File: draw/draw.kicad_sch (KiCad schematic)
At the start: 7 parts, among them J1 Screw_Terminal_01x03, U1 INA260

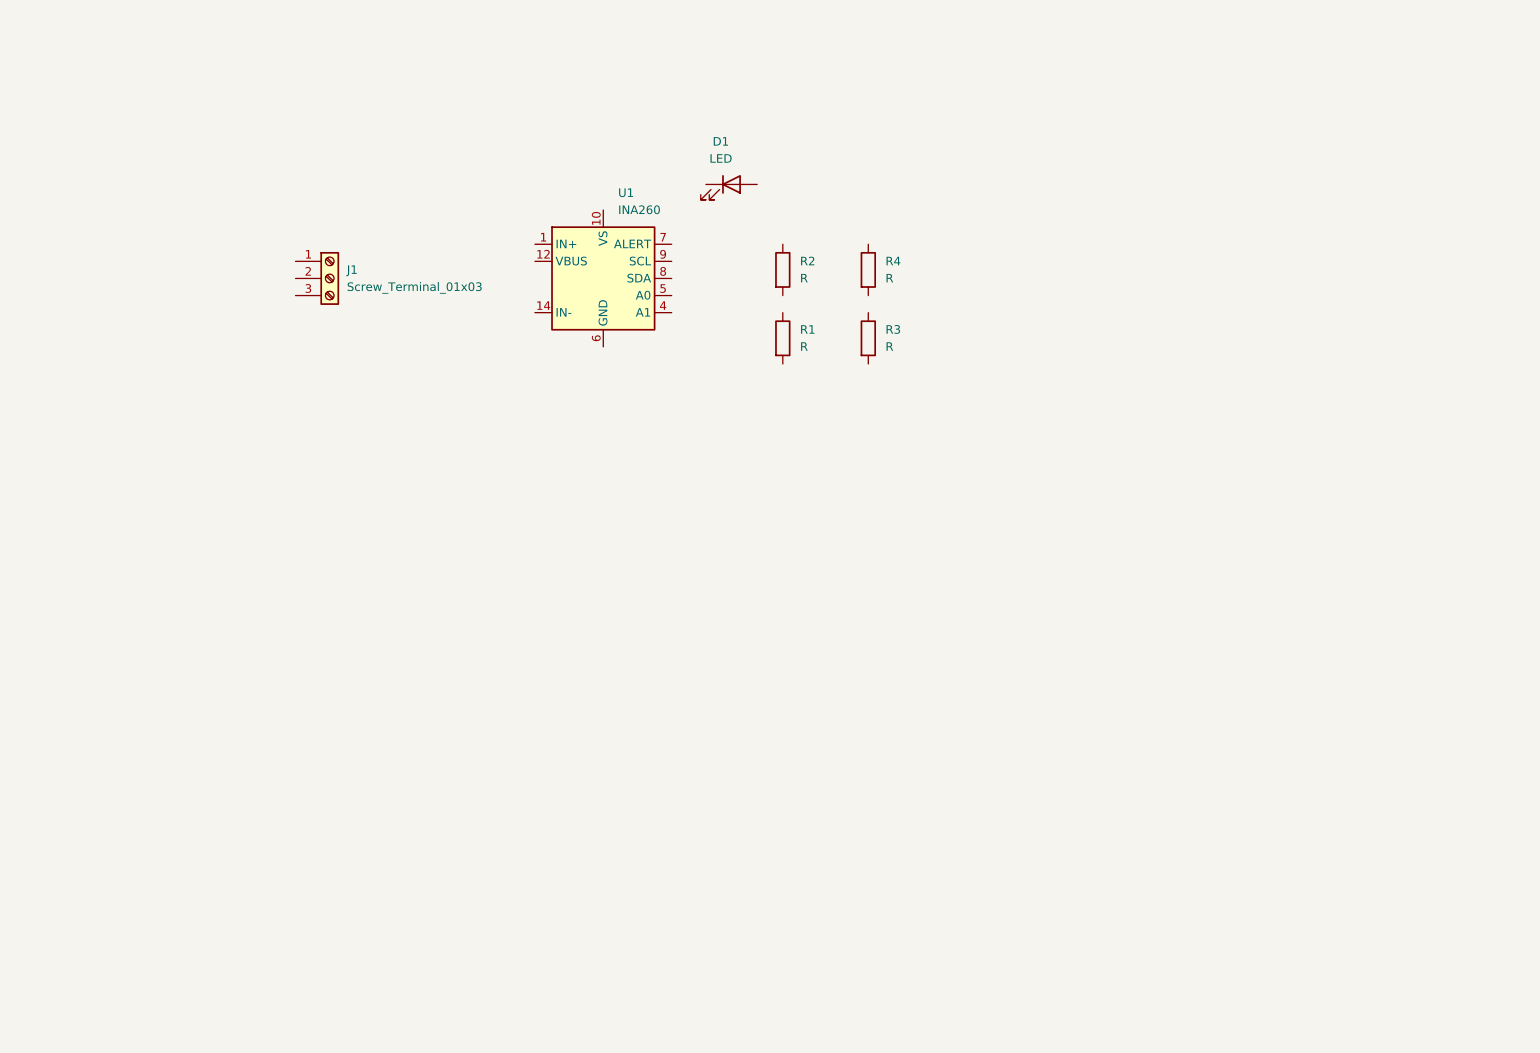
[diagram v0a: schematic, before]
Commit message: implemented schematic and pcb for draw v2
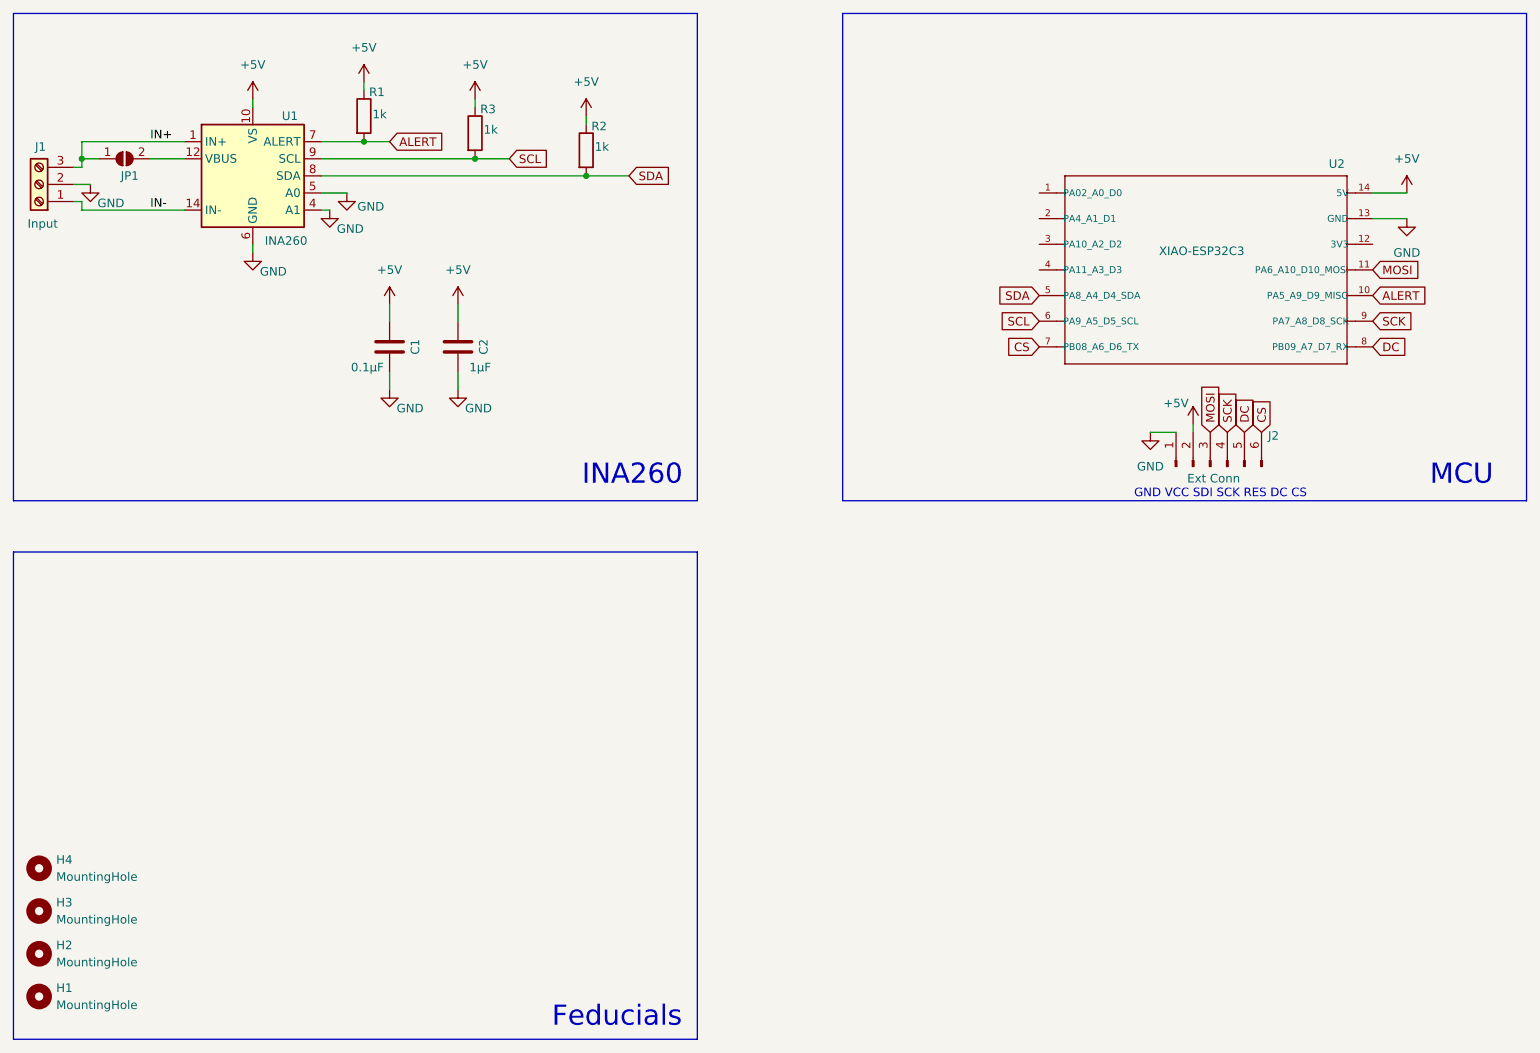
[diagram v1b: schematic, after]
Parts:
- removed D1: LED, symbol Device:LED
- removed R4: R, symbol Device:R
- added C1: 0.1µF, Capacitor_SMD:C_0805_2012Metric_Pad1.18x1.45mm_HandSolder, symbol Device:C
- added C2: 1µF, Capacitor_SMD:C_0805_2012Metric_Pad1.18x1.45mm_HandSolder, symbol Device:C
- added H1, H2, H3, H4: MountingHole, MountingHole:MountingHole_2.5mm, symbol Mechanical:MountingHole
- added J2: Ext Conn, Connector_PinHeader_2.54mm:PinHeader_1x06_P2.54mm_Vertical, symbol Connector:Conn_01x06_Pin
- added JP1: SolderJumper_2_Open, Jumper:SolderJumper-2_P1.3mm_Open_TrianglePad1.0x1.5mm, symbol Jumper:SolderJumper_2_Open
- added U2: XIAO-ESP32C3, SeeedStudio:MOUDLE14P-SMD-2.54-21X17.8MM, symbol SeeedStudio Xiao:MOUDLE-SEEEDUINO-XIAO-ESP32C3
- J1: value Screw_Terminal_01x03 -> Input; footprint (none) -> TerminalBlock_Phoenix:TerminalBlock_Phoenix_MPT-0,5-3-2.54_1x03_P2.54mm_Horizontal
- R1, R2, R3: value R -> 1k; footprint (none) -> Resistor_SMD:R_0805_2012Metric_Pad1.20x1.40mm_HandSolder
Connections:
- net IN+: now reaches U1.1 (IN+), U1.2 (IN+), U1.3 (IN+)
- net IN+: now also J1.3 (Pin_3), JP1.1 (A)
- net +5V: now reaches U1.10 (VS)
- net +5V: now also R1.1, R2.1, R3.1, C1.1, C2.1, J2.2 (Pin_2), U2.14 (5V)
- net GND: now reaches U1.11 (GND), U1.6 (GND)
- net GND: now also J1.2 (Pin_2), U1.4 (A1), U1.5 (A0), C1.2, C2.2, J2.1 (Pin_1), U2.13 (GND)
- net at U1.12 (VBUS): now also JP1.2 (B)
- net IN-: now reaches U1.14 (IN-), U1.15 (IN-), U1.16 (IN-)
- net IN-: now also J1.1 (Pin_1)
- net ALERT: now reaches U1.7 (ALERT)
- net ALERT: now also R1.2, U2.10 (PA5_A9_D9_MISO)
- net SDA: now reaches U1.8 (SDA)
- net SDA: now also R2.2, U2.5 (PA8_A4_D4_SDA)
- net SCL: now reaches U1.9 (SCL)
- net SCL: now also R3.2, U2.6 (PA9_A5_D5_SCL)
- new net CS: J2.6 (Pin_6), U2.7 (PB08_A6_D6_TX)
- new net DC: J2.5 (Pin_5), U2.8 (PB09_A7_D7_RX)
- new net MOSI: J2.3 (Pin_3), U2.11 (PA6_A10_D10_MOSI)
- new net SCK: J2.4 (Pin_4), U2.9 (PA7_A8_D8_SCK)
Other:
- note added: "Feducials"
- note added: "GND VCC SDI SCK RES DC CS"
- note added: "INA260"
- note added: "MCU"
- moved on the sheet: J1, U1
